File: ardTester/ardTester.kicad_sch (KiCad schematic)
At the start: 9 parts, among them U1 Arduino_Mini_Pro, U2 Power In, U3 Arduino_Mini_Pro

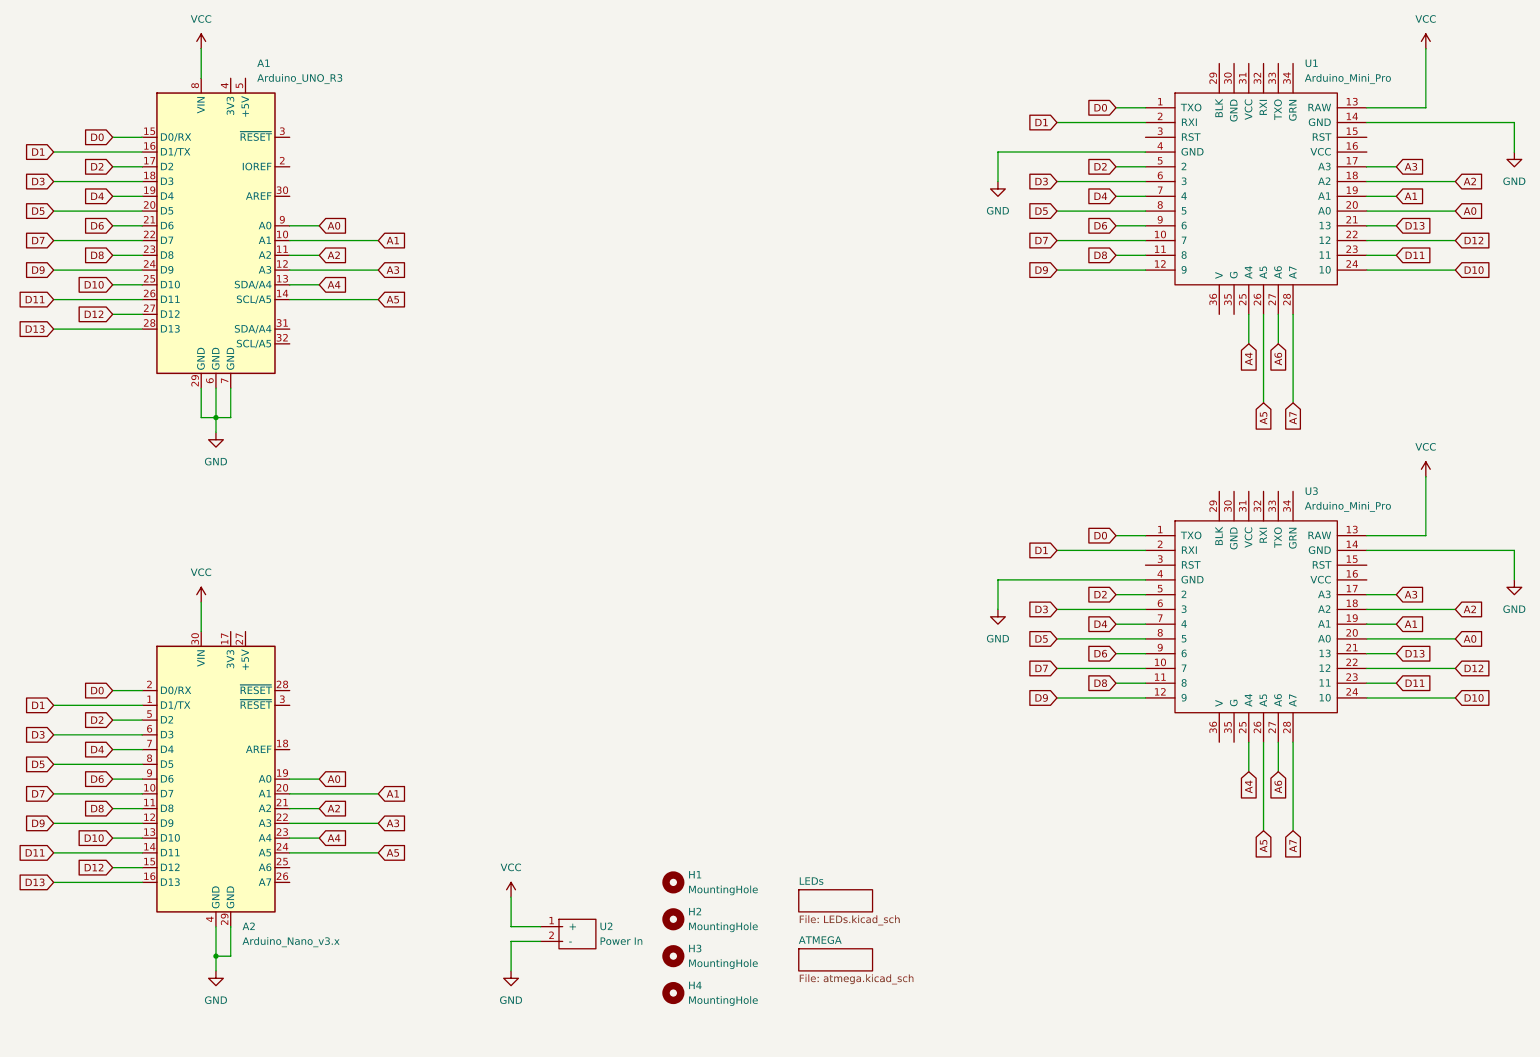
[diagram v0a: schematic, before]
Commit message: atmega/arduino tester
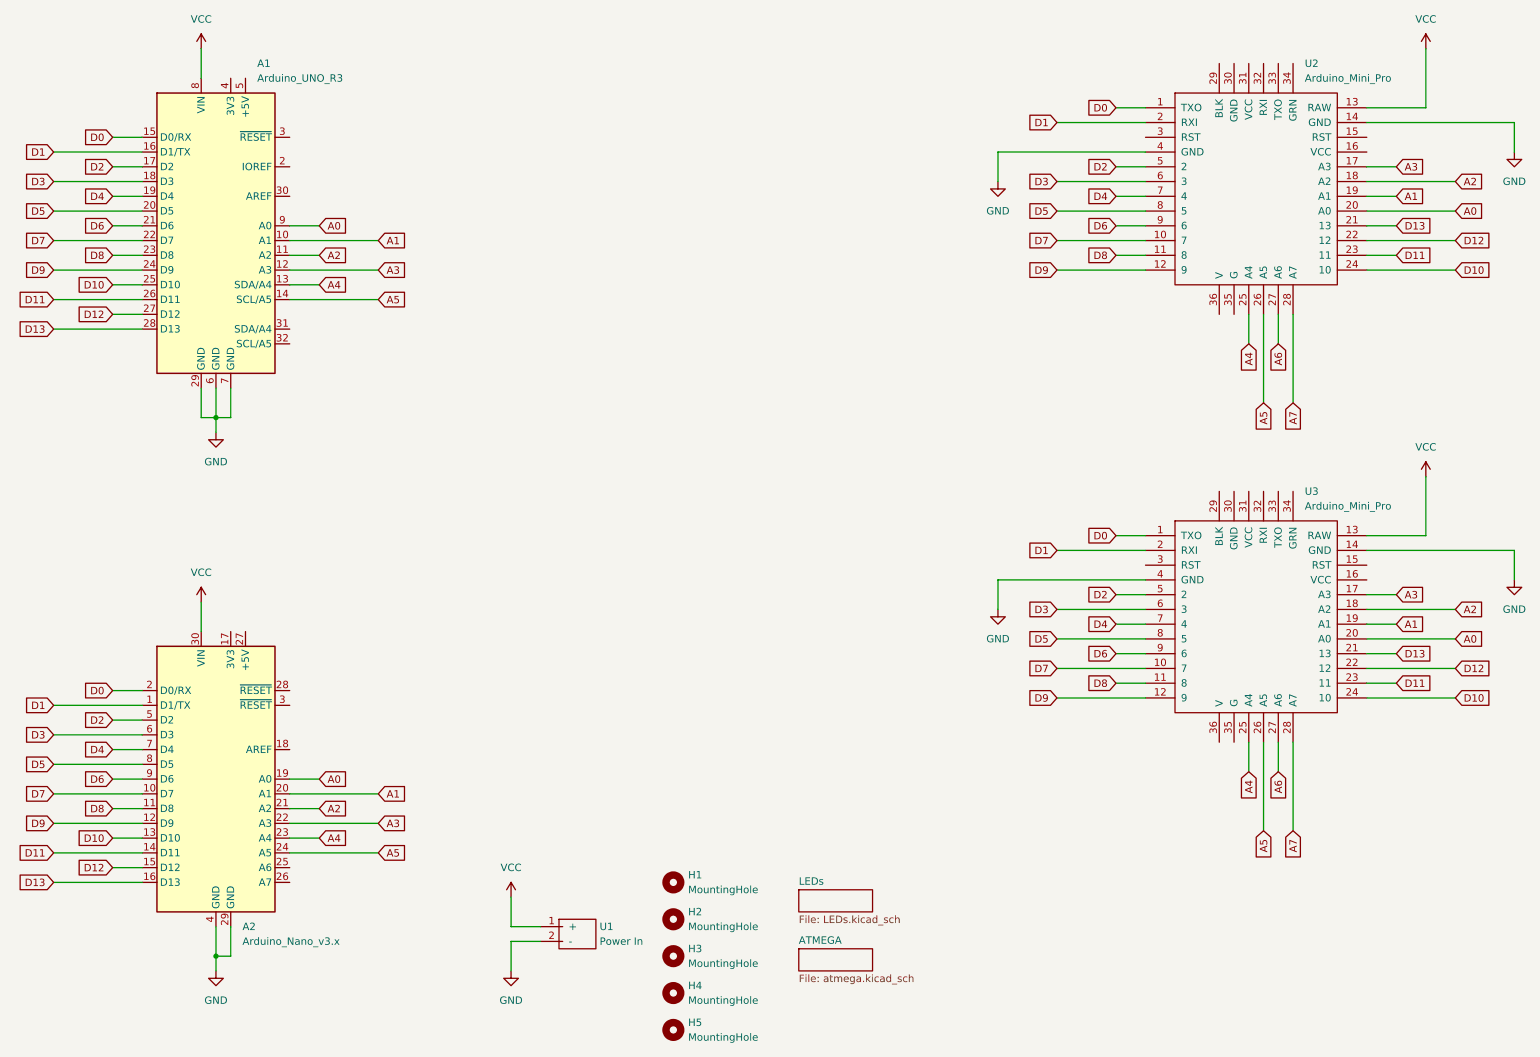
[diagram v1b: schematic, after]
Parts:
- added H5: MountingHole, MountingHole:MountingHole_3.2mm_M3, symbol Mechanical:MountingHole
- renumbered U2 to U1, U1 to U2
